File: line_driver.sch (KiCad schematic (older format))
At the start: 30 parts, among them J7 DRV632

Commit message: Fix 3D model scale for some caps.
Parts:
- C11, C15, C19, C22: footprint Capacitors_THT:CP_Radial_D4.0mm_P1.50mm -> blubaru:CP_Radial_D4.0mm_P1.50mm
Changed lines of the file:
@@
 F 0 "C11" H 4825 1900 50  0000 L CNN
 F 1 "1uF" H 4825 1700 50  0000 L CNN
-F 2 "Capacitors_THT:CP_Radial_D4.0mm_P1.50mm" H 4838 1650 50  0001 C CNN
+F 2 "blubaru:CP_Radial_D4.0mm_P1.50mm" H 4838 1650 50  0001 C CNN
 F 3 "http://www.nichicon.co.jp/english/products/pdfs/e-usw.pdf" H 4800 1800 50  0001 C CNN
 	1    4800 1800
@@
 F 0 "C15" H 5325 1900 50  0000 L CNN
 F 1 "1uF" H 5325 1700 50  0000 L CNN
-F 2 "Capacitors_THT:CP_Radial_D4.0mm_P1.50mm" H 5338 1650 50  0001 C CNN
+F 2 "blubaru:CP_Radial_D4.0mm_P1.50mm" H 5338 1650 50  0001 C CNN
 F 3 "http://www.nichicon.co.jp/english/products/pdfs/e-usw.pdf" H 5300 1800 50  0001 C CNN
 	1    5300 1800
@@
 F 0 "C19" H 6325 1900 50  0000 L CNN
 F 1 "1uF" H 6325 1700 50  0000 L CNN
-F 2 "Capacitors_THT:CP_Radial_D4.0mm_P1.50mm" H 6338 1650 50  0001 C CNN
+F 2 "blubaru:CP_Radial_D4.0mm_P1.50mm" H 6338 1650 50  0001 C CNN
 F 3 "http://www.nichicon.co.jp/english/products/pdfs/e-usw.pdf" H 6300 1800 50  0001 C CNN
 	1    6300 1800
@@
 F 0 "C22" H 6825 1900 50  0000 L CNN
 F 1 "1uF" H 6825 1700 50  0000 L CNN
-F 2 "Capacitors_THT:CP_Radial_D4.0mm_P1.50mm" H 6838 1650 50  0001 C CNN
+F 2 "blubaru:CP_Radial_D4.0mm_P1.50mm" H 6838 1650 50  0001 C CNN
 F 3 "http://www.nichicon.co.jp/english/products/pdfs/e-usw.pdf" H 6800 1800 50  0001 C CNN
 	1    6800 1800

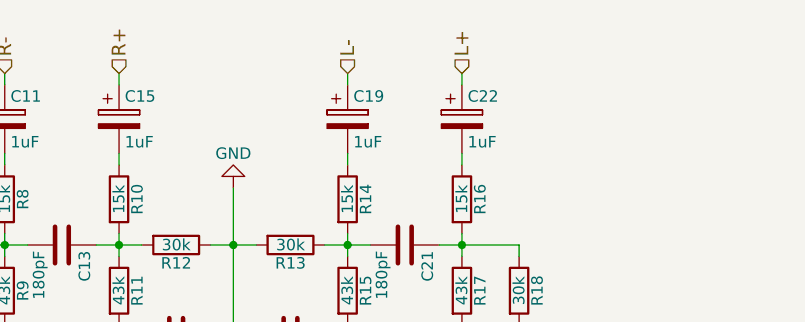
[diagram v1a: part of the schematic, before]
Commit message: Fix labels and lay resistors flat.
Left inputs to the line driver were backwards, because the datasheet had
an error. I think I "fixed"it before to match the datasheet.

I also decided to lay the resistors flat. They don't take up that much
room flat, and they will be easier to make pretty on the board, and more
stable with all the vibration.

Also updated the BOM and netlist.
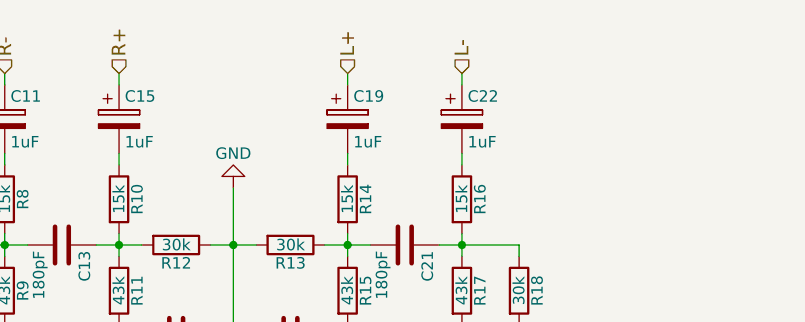
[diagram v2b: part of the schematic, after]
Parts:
- R10, R11, R12, R13, R14, R15, R16, R17, R18, R19, R6, R7, R8, R9: footprint Resistors_THT:R_Axial_DIN0204_L3.6mm_D1.6mm_P1.90mm_Vertical -> Resistors_THT:R_Axial_DIN0204_L3.6mm_D1.6mm_P5.08mm_Horizontal
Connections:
- net L+: now also C19.1; no longer C22.1
- net L-: now also C22.1; no longer C19.1
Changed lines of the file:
@@
 F 0 "R12" V 5630 2350 50  0000 C CNN
 F 1 "30k" V 5550 2350 50  0000 C CNN
-F 2 "Resistors_THT:R_Axial_DIN0204_L3.6mm_D1.6mm_P1.90mm_Vertical" V 5480 2350 50  0001 C CNN
+F 2 "Resistors_THT:R_Axial_DIN0204_L3.6mm_D1.6mm_P5.08mm_Horizontal" V 5480 2350 50  0001 C CNN
 F 3 "https://www.seielect.com/Catalog/SEI-RNF_RNMF.pdf" H 5550 2350 50  0001 C CNN
 	1    5550 2350
@@
 F 0 "R13" V 6130 2350 50  0000 C CNN
 F 1 "30k" V 6050 2350 50  0000 C CNN
-F 2 "Resistors_THT:R_Axial_DIN0204_L3.6mm_D1.6mm_P1.90mm_Vertical" V 5980 2350 50  0001 C CNN
+F 2 "Resistors_THT:R_Axial_DIN0204_L3.6mm_D1.6mm_P5.08mm_Horizontal" V 5980 2350 50  0001 C CNN
 F 3 "https://www.seielect.com/Catalog/SEI-RNF_RNMF.pdf" H 6050 2350 50  0001 C CNN
 	1    6050 2350
@@
 F 0 "R15" V 6380 2550 50  0000 C CNN
 F 1 "43k" V 6300 2550 50  0000 C CNN
-F 2 "Resistors_THT:R_Axial_DIN0204_L3.6mm_D1.6mm_P1.90mm_Vertical" V 6230 2550 50  0001 C CNN
+F 2 "Resistors_THT:R_Axial_DIN0204_L3.6mm_D1.6mm_P5.08mm_Horizontal" V 6230 2550 50  0001 C CNN
 F 3 "https://www.seielect.com/Catalog/SEI-RNF_RNMF.pdf" H 6300 2550 50  0001 C CNN
 	1    6300 2550
@@
 F 0 "R11" V 5380 2550 50  0000 C CNN
 F 1 "43k" V 5300 2550 50  0000 C CNN
-F 2 "Resistors_THT:R_Axial_DIN0204_L3.6mm_D1.6mm_P1.90mm_Vertical" V 5230 2550 50  0001 C CNN
+F 2 "Resistors_THT:R_Axial_DIN0204_L3.6mm_D1.6mm_P5.08mm_Horizontal" V 5230 2550 50  0001 C CNN
 F 3 "https://www.seielect.com/Catalog/SEI-RNF_RNMF.pdf" H 5300 2550 50  0001 C CNN
 	1    5300 2550
@@
 F 0 "R14" V 6380 2150 50  0000 C CNN
 F 1 "15k" V 6300 2150 50  0000 C CNN
-F 2 "Resistors_THT:R_Axial_DIN0204_L3.6mm_D1.6mm_P1.90mm_Vertical" V 6230 2150 50  0001 C CNN
+F 2 "Resistors_THT:R_Axial_DIN0204_L3.6mm_D1.6mm_P5.08mm_Horizontal" V 6230 2150 50  0001 C CNN
 F 3 "https://www.seielect.com/Catalog/SEI-RNF_RNMF.pdf" H 6300 2150 50  0001 C CNN
 	1    6300 2150
@@
 F 0 "R10" V 5380 2150 50  0000 C CNN
 F 1 "15k" V 5300 2150 50  0000 C CNN
-F 2 "Resistors_THT:R_Axial_DIN0204_L3.6mm_D1.6mm_P1.90mm_Vertical" V 5230 2150 50  0001 C CNN
+F 2 "Resistors_THT:R_Axial_DIN0204_L3.6mm_D1.6mm_P5.08mm_Horizontal" V 5230 2150 50  0001 C CNN
 F 3 "https://www.seielect.com/Catalog/SEI-RNF_RNMF.pdf" H 5300 2150 50  0001 C CNN
 	1    5300 2150
@@
 F 0 "R17" V 6880 2550 50  0000 C CNN
 F 1 "43k" V 6800 2550 50  0000 C CNN
-F 2 "Resistors_THT:R_Axial_DIN0204_L3.6mm_D1.6mm_P1.90mm_Vertical" V 6730 2550 50  0001 C CNN
+F 2 "Resistors_THT:R_Axial_DIN0204_L3.6mm_D1.6mm_P5.08mm_Horizontal" V 6730 2550 50  0001 C CNN
 F 3 "https://www.seielect.com/Catalog/SEI-RNF_RNMF.pdf" H 6800 2550 50  0001 C CNN
 	1    6800 2550
@@
 F 0 "R9" V 4880 2550 50  0000 C CNN
 F 1 "43k" V 4800 2550 50  0000 C CNN
-F 2 "Resistors_THT:R_Axial_DIN0204_L3.6mm_D1.6mm_P1.90mm_Vertical" V 4730 2550 50  0001 C CNN
+F 2 "Resistors_THT:R_Axial_DIN0204_L3.6mm_D1.6mm_P5.08mm_Horizontal" V 4730 2550 50  0001 C CNN
 F 3 "https://www.seielect.com/Catalog/SEI-RNF_RNMF.pdf" H 4800 2550 50  0001 C CNN
 	1    4800 2550
@@
 F 0 "R16" V 6880 2150 50  0000 C CNN
 F 1 "15k" V 6800 2150 50  0000 C CNN
-F 2 "Resistors_THT:R_Axial_DIN0204_L3.6mm_D1.6mm_P1.90mm_Vertical" V 6730 2150 50  0001 C CNN
+F 2 "Resistors_THT:R_Axial_DIN0204_L3.6mm_D1.6mm_P5.08mm_Horizontal" V 6730 2150 50  0001 C CNN
 F 3 "https://www.seielect.com/Catalog/SEI-RNF_RNMF.pdf" H 6800 2150 50  0001 C CNN
 	1    6800 2150
@@
 F 0 "R8" V 4880 2150 50  0000 C CNN
 F 1 "15k" V 4800 2150 50  0000 C CNN
-F 2 "Resistors_THT:R_Axial_DIN0204_L3.6mm_D1.6mm_P1.90mm_Vertical" V 4730 2150 50  0001 C CNN
+F 2 "Resistors_THT:R_Axial_DIN0204_L3.6mm_D1.6mm_P5.08mm_Horizontal" V 4730 2150 50  0001 C CNN
 F 3 "https://www.seielect.com/Catalog/SEI-RNF_RNMF.pdf" H 4800 2150 50  0001 C CNN
 	1    4800 2150
@@
 F 0 "R18" V 7130 2550 50  0000 C CNN
 F 1 "30k" V 7050 2550 50  0000 C CNN
-F 2 "Resistors_THT:R_Axial_DIN0204_L3.6mm_D1.6mm_P1.90mm_Vertical" V 6980 2550 50  0001 C CNN
+F 2 "Resistors_THT:R_Axial_DIN0204_L3.6mm_D1.6mm_P5.08mm_Horizontal" V 6980 2550 50  0001 C CNN
 F 3 "https://www.seielect.com/Catalog/SEI-RNF_RNMF.pdf" H 7050 2550 50  0001 C CNN
 	1    7050 2550
@@
 F 0 "R7" V 4630 2550 50  0000 C CNN
 F 1 "30k" V 4550 2550 50  0000 C CNN
-F 2 "Resistors_THT:R_Axial_DIN0204_L3.6mm_D1.6mm_P1.90mm_Vertical" V 4480 2550 50  0001 C CNN
+F 2 "Resistors_THT:R_Axial_DIN0204_L3.6mm_D1.6mm_P5.08mm_Horizontal" V 4480 2550 50  0001 C CNN
 F 3 "https://www.seielect.com/Catalog/SEI-RNF_RNMF.pdf" H 4550 2550 50  0001 C CNN
 	1    4550 2550
@@
 	7050 2700 7050 3300
 Connection ~ 7050 3300
+Text HLabel 6800 1600 1    60   Input ~ 0
+L-
 Text HLabel 6300 1600 1    60   Input ~ 0
-L-
-Text HLabel 6800 1600 1    60   Input ~ 0
 L+
 Text HLabel 4800 1600 1    60   Input ~ 0
@@
 F 0 "R19" V 7330 3300 50  0000 C CNN
 F 1 "33" V 7250 3300 50  0000 C CNN
-F 2 "Resistors_THT:R_Axial_DIN0204_L3.6mm_D1.6mm_P1.90mm_Vertical" V 7180 3300 50  0001 C CNN
+F 2 "Resistors_THT:R_Axial_DIN0204_L3.6mm_D1.6mm_P5.08mm_Horizontal" V 7180 3300 50  0001 C CNN
 F 3 "https://www.seielect.com/Catalog/SEI-RNF_RNMF.pdf" H 7250 3300 50  0001 C CNN
 	1    7250 3300
@@
 F 0 "R6" V 4430 3300 50  0000 C CNN
 F 1 "33" V 4350 3300 50  0000 C CNN
-F 2 "Resistors_THT:R_Axial_DIN0204_L3.6mm_D1.6mm_P1.90mm_Vertical" V 4280 3300 50  0001 C CNN
+F 2 "Resistors_THT:R_Axial_DIN0204_L3.6mm_D1.6mm_P5.08mm_Horizontal" V 4280 3300 50  0001 C CNN
 F 3 "https://www.seielect.com/Catalog/SEI-RNF_RNMF.pdf" H 4350 3300 50  0001 C CNN
 	1    4350 3300

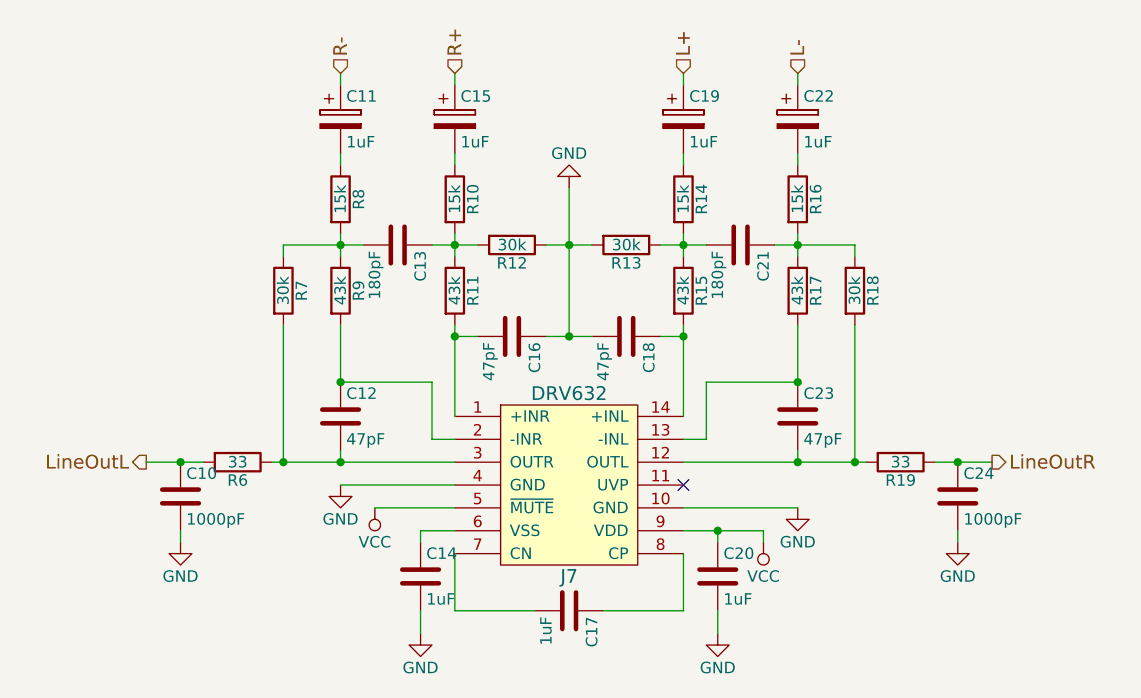
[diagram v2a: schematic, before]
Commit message: Add a line in module and use a smaller jack.
Lots of changes:
Added a line in. This requires another audio switch, so that's added to
the audio switch module.
Also, since I'm using two jacks, I chose a smaller jack module. This
needed a new footprint, and a new 3d model. The footprint is trickier,
since it really needed slots, which OSH won't guarantee. I've given it a
unique footprint to try to optimize the pad size around the edges of the
pins.
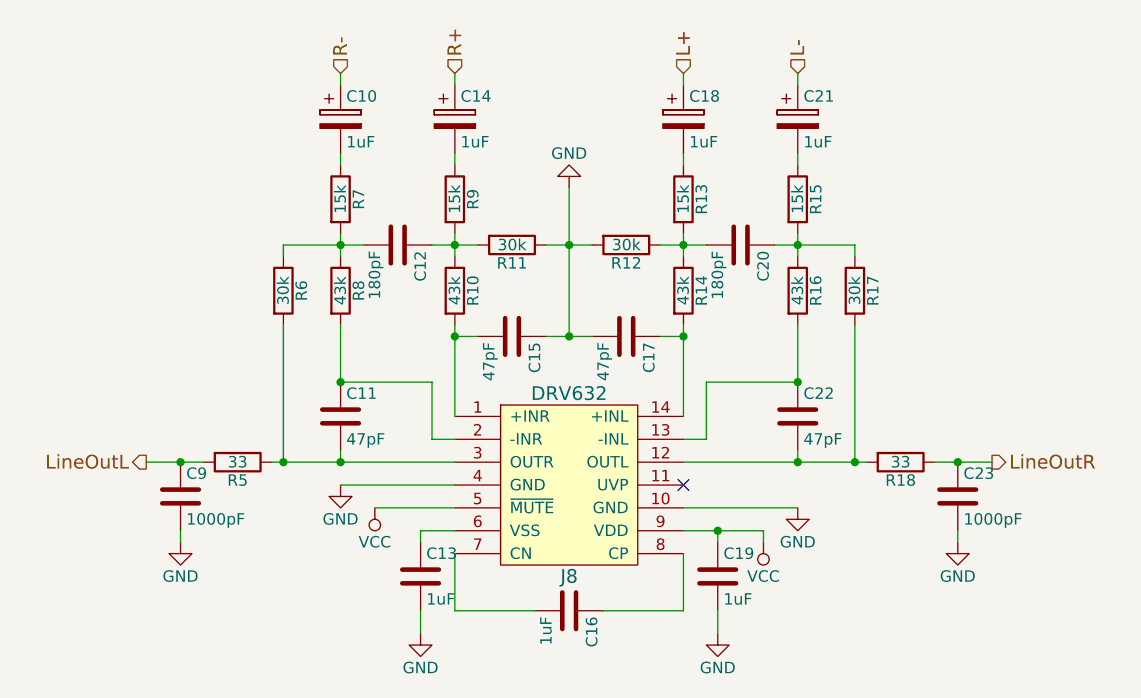
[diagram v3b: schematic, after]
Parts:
- renumbered C11 to C10, C12 to C11, C13 to C12, C14 to C13, C15 to C14, C16 to C15, C17 to C16, C18 to C17, C19 to C18, C20 to C19, C21 to C20, C22 to C21, C23 to C22, C24 to C23, C10 to C9, J7 to J8, R11 to R10, R12 to R11, R13 to R12, R14 to R13, R15 to R14, R16 to R15, R17 to R16, R18 to R17, R19 to R18, R6 to R5, R7 to R6, R8 to R7, R9 to R8, R10 to R9
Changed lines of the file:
@@
 $Descr A4 11693 8268
 encoding utf-8
-Sheet 8 8
+Sheet 8 10
 Title ""
 Date ""
@@
 $EndComp
 $Comp
-L C C17
+L C C16
 U 1 1 59178EA2
 P 5800 3950
-F 0 "C17" H 5825 4050 50  0000 L CNN
+F 0 "C16" H 5825 4050 50  0000 L CNN
 F 1 "1uF" H 5825 3850 50  0000 L CNN
 F 2 "blubaru:C_Disc_D5.0mm_W3.2mm_P2.50mm" H 5838 3800 50  0001 C CNN
@@
 	6300 3500 6800 3500
 $Comp
-L C C14
+L C C13
 U 1 1 59178EFD
 P 5150 3800
-F 0 "C14" H 5175 3900 50  0000 L CNN
+F 0 "C13" H 5175 3900 50  0000 L CNN
 F 1 "1uF" H 5175 3700 50  0000 L CNN
 F 2 "blubaru:C_Disc_D5.0mm_W3.2mm_P2.50mm" H 5188 3650 50  0001 C CNN
@@
 	5150 3950 5150 4050
 $Comp
-L C C20
+L C C19
 U 1 1 59178FC9
 P 6450 3800
-F 0 "C20" H 6475 3900 50  0000 L CNN
+F 0 "C19" H 6475 3900 50  0000 L CNN
 F 1 "1uF" H 6475 3700 50  0000 L CNN
 F 2 "blubaru:C_Disc_D5.0mm_W3.2mm_P2.50mm" H 6488 3650 50  0001 C CNN
@@
 LineOutL
 $Comp
-L C C23
+L C C22
 U 1 1 59179109
 P 6800 3100
-F 0 "C23" H 6825 3200 50  0000 L CNN
+F 0 "C22" H 6825 3200 50  0000 L CNN
 F 1 "47pF" H 6825 3000 50  0000 L CNN
 F 2 "blubaru:C_Disc_D4.0mm_W2.6mm_P2.50mm" H 6838 2950 50  0001 C CNN
@@
 $EndComp
 $Comp
-L C C12
+L C C11
 U 1 1 5917915A
 P 4800 3100
-F 0 "C12" H 4825 3200 50  0000 L CNN
+F 0 "C11" H 4825 3200 50  0000 L CNN
 F 1 "47pF" H 4825 3000 50  0000 L CNN
 F 2 "blubaru:C_Disc_D4.0mm_W2.6mm_P2.50mm" H 4838 2950 50  0001 C CNN
@@
 	6400 3200 6300 3200
 $Comp
-L C C18
+L C C17
 U 1 1 591791B6
 P 6050 2750
-F 0 "C18" H 6075 2850 50  0000 L CNN
+F 0 "C17" H 6075 2850 50  0000 L CNN
 F 1 "47pF" H 6075 2650 50  0000 L CNN
 F 2 "blubaru:C_Disc_D4.0mm_W2.6mm_P2.50mm" H 6088 2600 50  0001 C CNN
@@
 $EndComp
 $Comp
-L C C16
+L C C15
 U 1 1 591791EB
 P 5550 2750
-F 0 "C16" H 5575 2850 50  0000 L CNN
+F 0 "C15" H 5575 2850 50  0000 L CNN
 F 1 "47pF" H 5575 2650 50  0000 L CNN
 F 2 "blubaru:C_Disc_D4.0mm_W2.6mm_P2.50mm" H 5588 2600 50  0001 C CNN
@@
 $EndComp
 $Comp
-L R R12
+L R R11
 U 1 1 59179216
 P 5550 2350
-F 0 "R12" V 5630 2350 50  0000 C CNN
+F 0 "R11" V 5630 2350 50  0000 C CNN
 F 1 "30k" V 5550 2350 50  0000 C CNN
 F 2 "Resistors_THT:R_Axial_DIN0204_L3.6mm_D1.6mm_P5.08mm_Horizontal" V 5480 2350 50  0001 C CNN
@@
 $EndComp
 $Comp
-L R R13
+L R R12
 U 1 1 59179241
 P 6050 2350
-F 0 "R13" V 6130 2350 50  0000 C CNN
+F 0 "R12" V 6130 2350 50  0000 C CNN
 F 1 "30k" V 6050 2350 50  0000 C CNN
 F 2 "Resistors_THT:R_Axial_DIN0204_L3.6mm_D1.6mm_P5.08mm_Horizontal" V 5980 2350 50  0001 C CNN
@@
 Connection ~ 5800 2350
 $Comp
-L R R15
+L R R14
 U 1 1 59179384
 P 6300 2550
-F 0 "R15" V 6380 2550 50  0000 C CNN
+F 0 "R14" V 6380 2550 50  0000 C CNN
 F 1 "43k" V 6300 2550 50  0000 C CNN
 F 2 "Resistors_THT:R_Axial_DIN0204_L3.6mm_D1.6mm_P5.08mm_Horizontal" V 6230 2550 50  0001 C CNN
@@
 $EndComp
 $Comp
-L R R11
+L R R10
 U 1 1 591793C1
 P 5300 2550
-F 0 "R11" V 5380 2550 50  0000 C CNN
+F 0 "R10" V 5380 2550 50  0000 C CNN
 F 1 "43k" V 5300 2550 50  0000 C CNN
 F 2 "Resistors_THT:R_Axial_DIN0204_L3.6mm_D1.6mm_P5.08mm_Horizontal" V 5230 2550 50  0001 C CNN
@@
 	5300 2700 5300 3100
 $Comp
-L R R14
+L R R13
 U 1 1 5917A21C
 P 6300 2150
-F 0 "R14" V 6380 2150 50  0000 C CNN
+F 0 "R13" V 6380 2150 50  0000 C CNN
 F 1 "15k" V 6300 2150 50  0000 C CNN
 F 2 "Resistors_THT:R_Axial_DIN0204_L3.6mm_D1.6mm_P5.08mm_Horizontal" V 6230 2150 50  0001 C CNN
@@
 $EndComp
 $Comp
-L R R10
+L R R9
 U 1 1 5917A253
 P 5300 2150
-F 0 "R10" V 5380 2150 50  0000 C CNN
+F 0 "R9" V 5380 2150 50  0000 C CNN
 F 1 "15k" V 5300 2150 50  0000 C CNN
 F 2 "Resistors_THT:R_Axial_DIN0204_L3.6mm_D1.6mm_P5.08mm_Horizontal" V 5230 2150 50  0001 C CNN
@@
 	5300 1950 5300 2000
 $Comp
-L C C13
+L C C12
 U 1 1 5917A56B
 P 5050 2350
-F 0 "C13" H 5075 2450 50  0000 L CNN
+F 0 "C12" H 5075 2450 50  0000 L CNN
 F 1 "180pF" H 5075 2250 50  0000 L CNN
 F 2 "blubaru:C_Disc_D4.0mm_W2.6mm_P2.50mm" H 5088 2200 50  0001 C CNN
@@
 $EndComp
 $Comp
-L C C21
+L C C20
 U 1 1 5917A5AC
 P 6550 2350
-F 0 "C21" H 6575 2450 50  0000 L CNN
+F 0 "C20" H 6575 2450 50  0000 L CNN
 F 1 "180pF" H 6575 2250 50  0000 L CNN
 F 2 "blubaru:C_Disc_D4.0mm_W2.6mm_P2.50mm" H 6588 2200 50  0001 C CNN
@@
 	6700 2350 7050 2350
 $Comp
-L R R17
+L R R16
 U 1 1 5917A8A8
 P 6800 2550
-F 0 "R17" V 6880 2550 50  0000 C CNN
+F 0 "R16" V 6880 2550 50  0000 C CNN
 F 1 "43k" V 6800 2550 50  0000 C CNN
 F 2 "Resistors_THT:R_Axial_DIN0204_L3.6mm_D1.6mm_P5.08mm_Horizontal" V 6730 2550 50  0001 C CNN
@@
 $EndComp
 $Comp
-L R R9
+L R R8
 U 1 1 5917A8FF
 P 4800 2550
-F 0 "R9" V 4880 2550 50  0000 C CNN
+F 0 "R8" V 4880 2550 50  0000 C CNN
 F 1 "43k" V 4800 2550 50  0000 C CNN
 F 2 "Resistors_THT:R_Axial_DIN0204_L3.6mm_D1.6mm_P5.08mm_Horizontal" V 4730 2550 50  0001 C CNN
@@
 Connection ~ 4800 2350
 $Comp
-L R R16
+L R R15
 U 1 1 5917AA6A
 P 6800 2150
-F 0 "R16" V 6880 2150 50  0000 C CNN
+F 0 "R15" V 6880 2150 50  0000 C CNN
 F 1 "15k" V 6800 2150 50  0000 C CNN
 F 2 "Resistors_THT:R_Axial_DIN0204_L3.6mm_D1.6mm_P5.08mm_Horizontal" V 6730 2150 50  0001 C CNN
@@
 $EndComp
 $Comp
-L R R8
+L R R7
 U 1 1 5917AAD3
 P 4800 2150
-F 0 "R8" V 4880 2150 50  0000 C CNN
+F 0 "R7" V 4880 2150 50  0000 C CNN
 F 1 "15k" V 4800 2150 50  0000 C CNN
 F 2 "Resistors_THT:R_Axial_DIN0204_L3.6mm_D1.6mm_P5.08mm_Horizontal" V 4730 2150 50  0001 C CNN
@@
 Connection ~ 4800 2950
 $Comp
-L R R18
+L R R17
 U 1 1 5917AD17
 P 7050 2550
-F 0 "R18" V 7130 2550 50  0000 C CNN
+F 0 "R17" V 7130 2550 50  0000 C CNN
 F 1 "30k" V 7050 2550 50  0000 C CNN
 F 2 "Resistors_THT:R_Axial_DIN0204_L3.6mm_D1.6mm_P5.08mm_Horizontal" V 6980 2550 50  0001 C CNN
@@
 $EndComp
 $Comp
-L R R7
+L R R6
 U 1 1 5917AD78
 P 4550 2550
-F 0 "R7" V 4630 2550 50  0000 C CNN
+F 0 "R6" V 4630 2550 50  0000 C CNN
 F 1 "30k" V 4550 2550 50  0000 C CNN
 F 2 "Resistors_THT:R_Axial_DIN0204_L3.6mm_D1.6mm_P5.08mm_Horizontal" V 4480 2550 50  0001 C CNN
@@
 Connection ~ 5300 2750
 $Comp
-L DRV632 J7
+L DRV632 J8
 U 1 1 592F828F
 P 5800 3000
-F 0 "J7" H 5800 2200 60  0000 C CNN
+F 0 "J8" H 5800 2200 60  0000 C CNN
 F 1 "DRV632" H 5800 3000 60  0000 C CNN
 F 2 "blubaru:DRV632" H 5800 3000 60  0001 C CNN
@@
 $EndComp
 $Comp
-L C C24
+L C C23
 U 1 1 5933924A
 P 7500 3450
-F 0 "C24" H 7525 3550 50  0000 L CNN
+F 0 "C23" H 7525 3550 50  0000 L CNN
 F 1 "1000pF" H 7525 3350 50  0000 L CNN
 F 2 "blubaru:C_Disc_D4.0mm_W2.6mm_P2.50mm" H 7538 3300 50  0001 C CNN
@@
 $EndComp
 $Comp
-L C C10
+L C C9
 U 1 1 593392DF
 P 4100 3450
-F 0 "C10" H 4125 3550 50  0000 L CNN
+F 0 "C9" H 4125 3550 50  0000 L CNN
 F 1 "1000pF" H 4125 3350 50  0000 L CNN
 F 2 "blubaru:C_Disc_D4.0mm_W2.6mm_P2.50mm" H 4138 3300 50  0001 C CNN
@@
 $EndComp
 $Comp
-L R R19
+L R R18
 U 1 1 59339334
 P 7250 3300
-F 0 "R19" V 7330 3300 50  0000 C CNN
+F 0 "R18" V 7330 3300 50  0000 C CNN
 F 1 "33" V 7250 3300 50  0000 C CNN
 F 2 "Resistors_THT:R_Axial_DIN0204_L3.6mm_D1.6mm_P5.08mm_Horizontal" V 7180 3300 50  0001 C CNN
@@
 $EndComp
 $Comp
-L R R6
+L R R5
 U 1 1 593393C3
 P 4350 3300
-F 0 "R6" V 4430 3300 50  0000 C CNN
+F 0 "R5" V 4430 3300 50  0000 C CNN
 F 1 "33" V 4350 3300 50  0000 C CNN
 F 2 "Resistors_THT:R_Axial_DIN0204_L3.6mm_D1.6mm_P5.08mm_Horizontal" V 4280 3300 50  0001 C CNN
@@
 	4100 3600 4100 3650
 $Comp
-L CP C11
+L CP C10
 U 1 1 5939D955
 P 4800 1800
-F 0 "C11" H 4825 1900 50  0000 L CNN
+F 0 "C10" H 4825 1900 50  0000 L CNN
 F 1 "1uF" H 4825 1700 50  0000 L CNN
 F 2 "blubaru:CP_Radial_D4.0mm_P1.50mm" H 4838 1650 50  0001 C CNN
@@
 $EndComp
 $Comp
-L CP C15
+L CP C14
 U 1 1 5939DA1E
 P 5300 1800
-F 0 "C15" H 5325 1900 50  0000 L CNN
+F 0 "C14" H 5325 1900 50  0000 L CNN
 F 1 "1uF" H 5325 1700 50  0000 L CNN
 F 2 "blubaru:CP_Radial_D4.0mm_P1.50mm" H 5338 1650 50  0001 C CNN
@@
 $EndComp
 $Comp
-L CP C19
+L CP C18
 U 1 1 5939DA7F
 P 6300 1800
-F 0 "C19" H 6325 1900 50  0000 L CNN
+F 0 "C18" H 6325 1900 50  0000 L CNN
 F 1 "1uF" H 6325 1700 50  0000 L CNN
 F 2 "blubaru:CP_Radial_D4.0mm_P1.50mm" H 6338 1650 50  0001 C CNN
@@
 $EndComp
 $Comp
-L CP C22
+L CP C21
 U 1 1 5939DADA
 P 6800 1800
-F 0 "C22" H 6825 1900 50  0000 L CNN
+F 0 "C21" H 6825 1900 50  0000 L CNN
 F 1 "1uF" H 6825 1700 50  0000 L CNN
 F 2 "blubaru:CP_Radial_D4.0mm_P1.50mm" H 6838 1650 50  0001 C CNN
